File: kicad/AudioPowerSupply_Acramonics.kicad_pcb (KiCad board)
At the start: 2 copper layers, 33 parts, among them J6 GND 48V, J7 Conn_01x03_Pin, J8 Conn_01x03_Pin, U1 LM7815_TO220, U2 LM7915_TO220, U3 LM317_TO-220

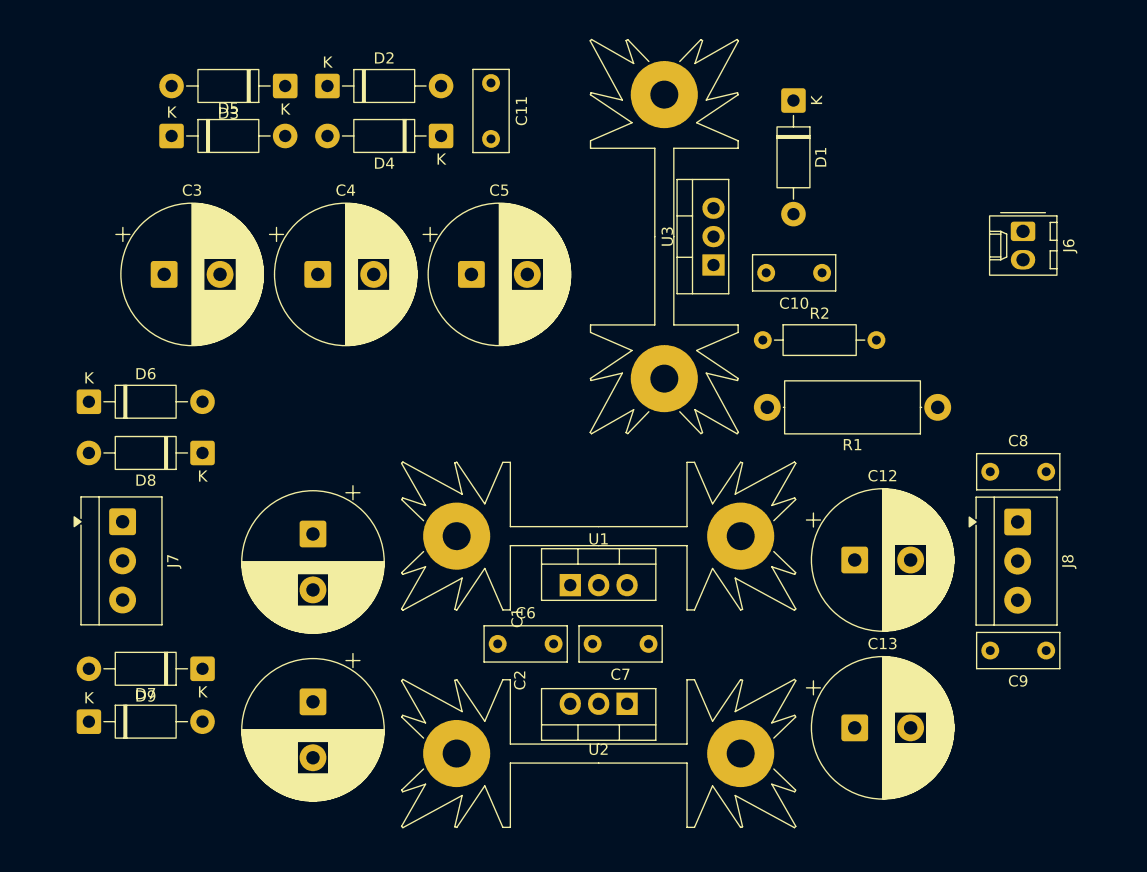
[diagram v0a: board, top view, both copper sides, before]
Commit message: Put 48V circuit on separate diagram
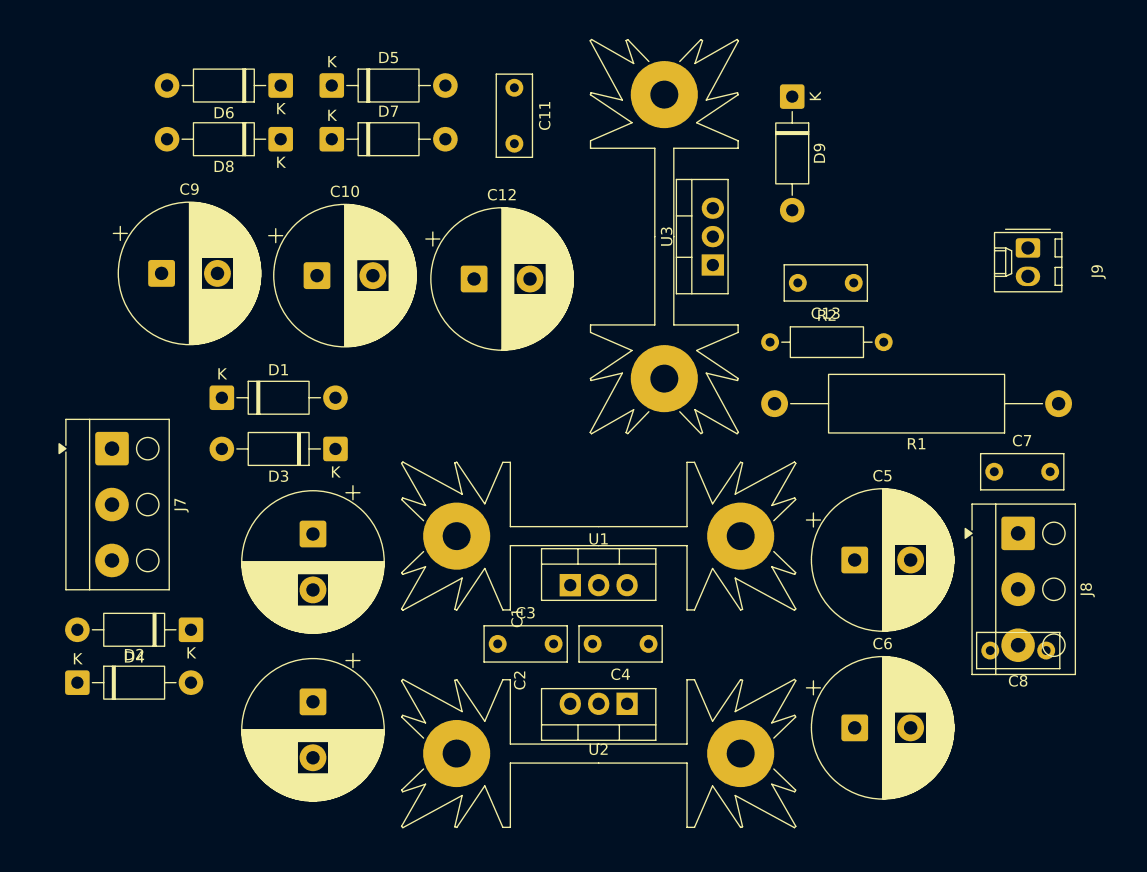
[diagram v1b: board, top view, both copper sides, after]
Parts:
- removed the C3 at (69.0, 88.7)
- removed the C4 at (82.7, 88.7)
- removed the C5 at (96.5, 88.7)
- removed the D1 at (125.3, 73.2)
- removed the D2 at (83.6, 71.9)
- removed the D3 at (79.8, 71.9)
- removed the D4 at (93.7, 76.4)
- removed J6: GND 48V, Connector_Molex:Molex_KK-254_AE-6410-02A_1x02_P2.54mm_Vertical
- added C12: 220uF 100V, Capacitor_THT:CP_Radial_D12.5mm_P5.00mm, F.Cu at (96.7, 89.2)
- added C13: 100nF, Capacitor_THT:C_Rect_L7.2mm_W3.0mm_P5.00mm_FKS2_FKP2_MKS2_MKP2, F.Cu at (130.7, 89.5)
- added C9: 100uF 100V, Capacitor_THT:CP_Radial_D12.5mm_P5.00mm, F.Cu at (68.8, 88.7)
- added D6: 1N4004, Diode_THT:D_DO-41_SOD81_P10.16mm_Horizontal, F.Cu at (79.4, 71.8)
- added D7: 1N4004, Diode_THT:D_DO-41_SOD81_P10.16mm_Horizontal, F.Cu at (84.0, 76.7)
- added D8: 1N4004, Diode_THT:D_DO-41_SOD81_P10.16mm_Horizontal, F.Cu at (79.4, 76.7)
- added D9: 1N4003, Diode_THT:D_DO-41_SOD81_P10.16mm_Horizontal, F.Cu at (125.2, 72.8)
- added J9: 48V out, Connector_Molex:Molex_KK-254_AE-6410-02A_1x02_P2.54mm_Vertical, F.Cu at (146.2, 86.4)
- C10: value 100nF -> 100uF 100V; footprint Capacitor_THT:C_Rect_L7.2mm_W3.0mm_P5.00mm_FKS2_FKP2_MKS2_MKP2 -> Capacitor_THT:CP_Radial_D12.5mm_P5.00mm
- J7, J8: footprint TerminalBlock_4Ucon:TerminalBlock_4Ucon_1x03_P3.50mm_Horizontal -> TerminalBlock_Altech:Altech_AK100_1x03_P5.00mm
- R1: footprint Resistor_THT:R_Axial_DIN0414_L11.9mm_D4.5mm_P15.24mm_Horizontal -> Resistor_THT:R_Axial_DIN0516_L15.5mm_D5.0mm_P25.40mm_Horizontal
- moved C10 45.2 mm to (82.7, 88.8), turned to 0 degrees
- moved D5 15.0 mm to (84.0, 71.8)
- moved D1 11.9 mm to (74.1, 99.8)
- moved D3 11.9 mm to (84.3, 104.3)
- moved R1 10.8 mm to (149.0, 100.3)
- moved J7 6.60 mm to (64.3, 104.3)
- moved D4 3.64 mm to (71.4, 120.5)
- moved D2 3.64 mm to (61.2, 125.2)
- moved C11 2.13 mm to (100.3, 72.0)
- moved J8 1.02 mm to (145.3, 111.9)
- moved R2 0.68 mm to (123.2, 94.8)
- moved C7 0.36 mm to (143.2, 106.4)
- moved U3 0.06 mm to (118.0, 87.9)
- renumbered C6 to C3, C7 to C4, C12 to C5, C13 to C6, C8 to C7, C9 to C8, D6 to D1, D7 to D2, D8 to D3, D9 to D4
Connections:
- C10 pad 1: GND -> Net-(D6-K)
- C10 pad 2: +48V -> AC17-

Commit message: Board done - needs added text
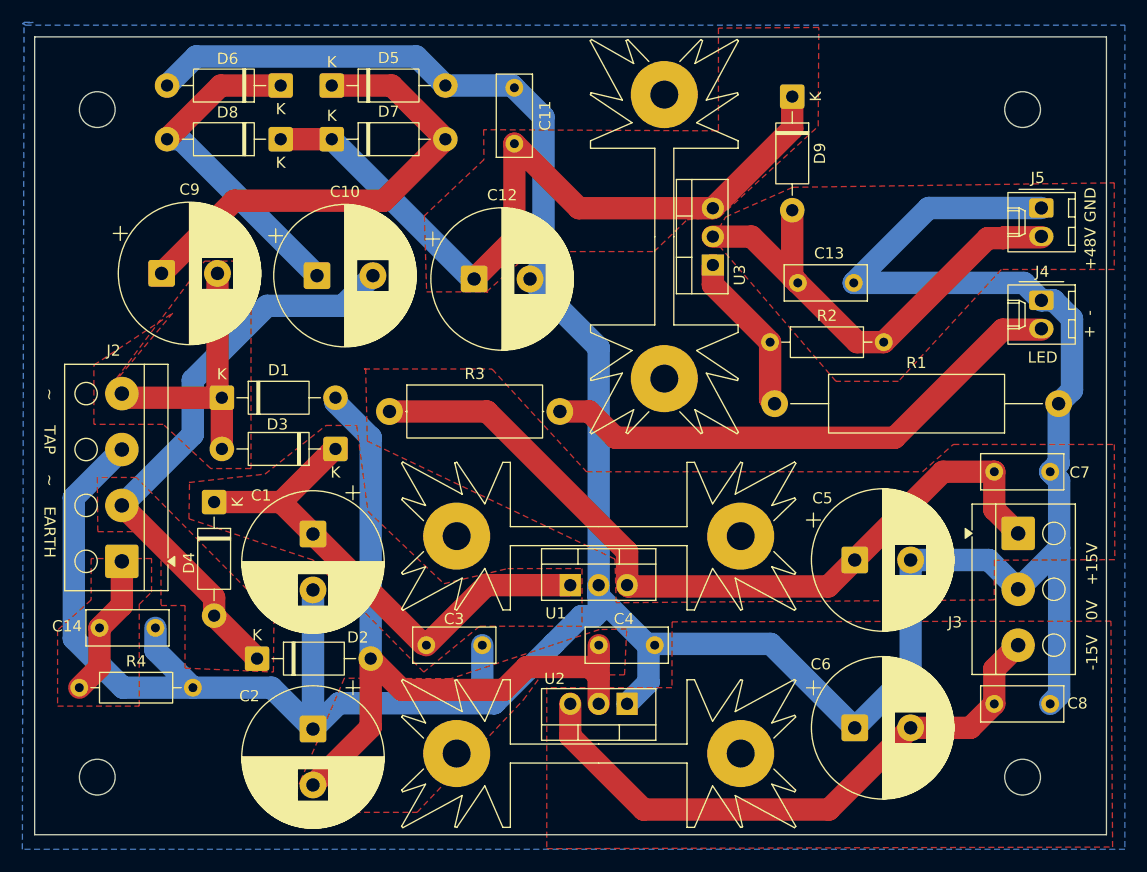
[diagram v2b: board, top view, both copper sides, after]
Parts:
- removed J7: Conn_01x03_Pin, TerminalBlock_Altech:Altech_AK100_1x03_P5.00mm
- added C14: 10nF, Capacitor_THT:C_Rect_L7.2mm_W3.0mm_P5.00mm_FKS2_FKP2_MKS2_MKP2, F.Cu at (63.2, 120.3)
- added J2: Conn_01x04_Pin, TerminalBlock_Altech:Altech_AK100_1x04_P5.00mm, F.Cu at (65.2, 114.4)
- added J4: ~, Connector_Molex:Molex_KK-254_AE-6410-02A_1x02_P2.54mm_Vertical, F.Cu at (147.4, 91.1)
- added R3: 3K6 1W, Resistor_THT:R_Axial_DIN0414_L11.9mm_D4.5mm_P15.24mm_Horizontal, F.Cu at (89.1, 101.0)
- added R4: 1K, Resistor_THT:R_Axial_DIN0207_L6.3mm_D2.5mm_P10.16mm_Horizontal, F.Cu at (61.4, 125.7)
- added REF**: MountingHole_3.2mm_M3, MountingHole:MountingHole_3.2mm_M3, F.Cu at (63.0, 74.0)
- added REF**: MountingHole_3.2mm_M3, MountingHole:MountingHole_3.2mm_M3, F.Cu at (145.8, 133.7)
- added REF**: MountingHole_3.2mm_M3, MountingHole:MountingHole_3.2mm_M3, F.Cu at (145.8, 74.0)
- added REF**: MountingHole_3.2mm_M3, MountingHole:MountingHole_3.2mm_M3, F.Cu at (63.0, 133.7)
- J3: renamed from J8; value Conn_01x03_Pin -> ~
- moved D2 16.2 mm to (77.3, 123.1)
- moved D4 11.6 mm to (73.5, 109.1), turned to -90 degrees
- moved C3 6.38 mm to (92.4, 121.9)
- moved C8 4.79 mm to (148.2, 127.2)
- moved J5 3.77 mm to (147.4, 82.8)
- moved C2 2.43 mm to (82.3, 129.4)
- moved C4 0.56 mm to (112.8, 121.9)
- renumbered J9 to J5
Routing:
- net GND: track 0.00 -> 326.6 mm
- net +15V: track 0.00 -> 73.0 mm
- net Net-(D7-K): track 0.00 -> 69.1 mm
- net Net-(D1-A): track 0.00 -> 66.0 mm
- net -15V: track 0.00 -> 53.6 mm
- net AC17-: track 0.00 -> 52.5 mm
- net Net-(J4-Pin_2): track 0.00 -> 48.0 mm
- net Net-(D3-K): track 0.00 -> 45.9 mm
- net +48V: track 0.00 -> 43.9 mm
- net Net-(D5-K): track 0.00 -> 42.5 mm
- net Net-(D6-K): track 0.00 -> 30.6 mm
- net AC17+: track 0.00 -> 25.0 mm
- net Net-(U3-ADJ): track 0.00 -> 14.7 mm
- net GNDPWR: track 0.00 -> 12.9 mm
- added copper zone on F.Cu, net +15V
- added copper zone on F.Cu, net +48V
- added copper zone on F.Cu, net -15V
- added copper zone on F.Cu, net AC17+
- added copper zone on F.Cu, net AC17-
- added copper zone on B.Cu, net GND
- added copper zone on F.Cu, net GNDPWR
- added copper zone on F.Cu, net Net-(D1-A)
- added copper zone on F.Cu, net Net-(D3-K)
- added copper zone on F.Cu, net Net-(D7-K)
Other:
- board outline added: 95.8 x 71.3 mm
- board text added: "+ -"
- board text added: "+48V GND"
- board text added: "-15V 0V +15V"
- board text added: "LED"
- board text added: "~ TAP ~ EARTH"

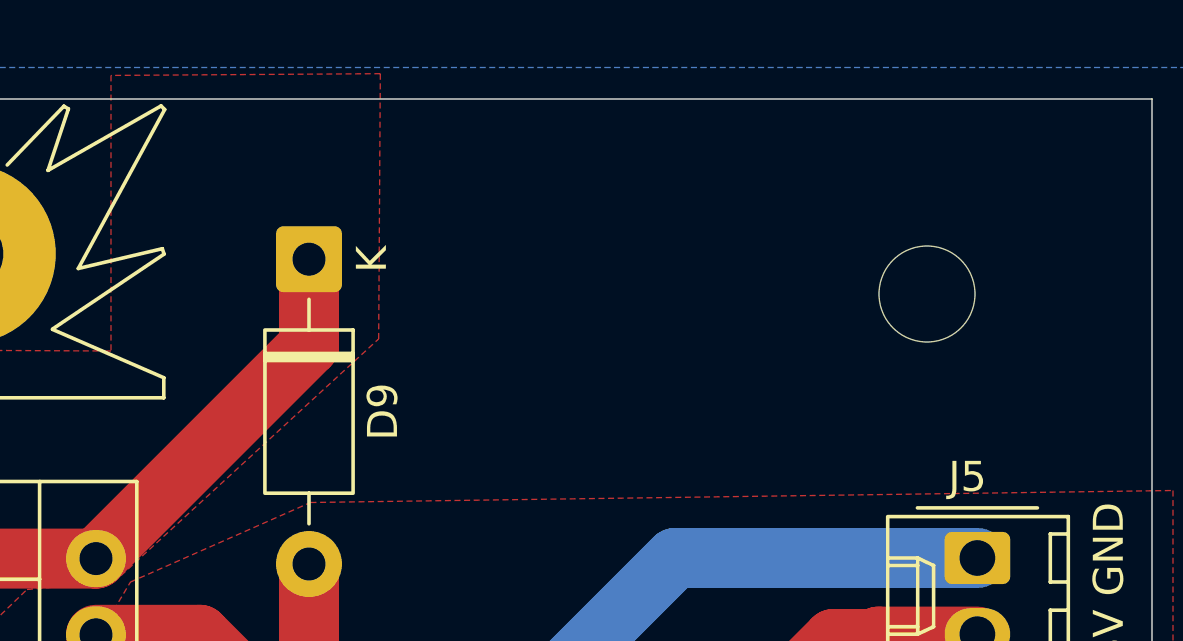
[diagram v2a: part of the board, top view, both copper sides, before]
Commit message: Added text and updated readme
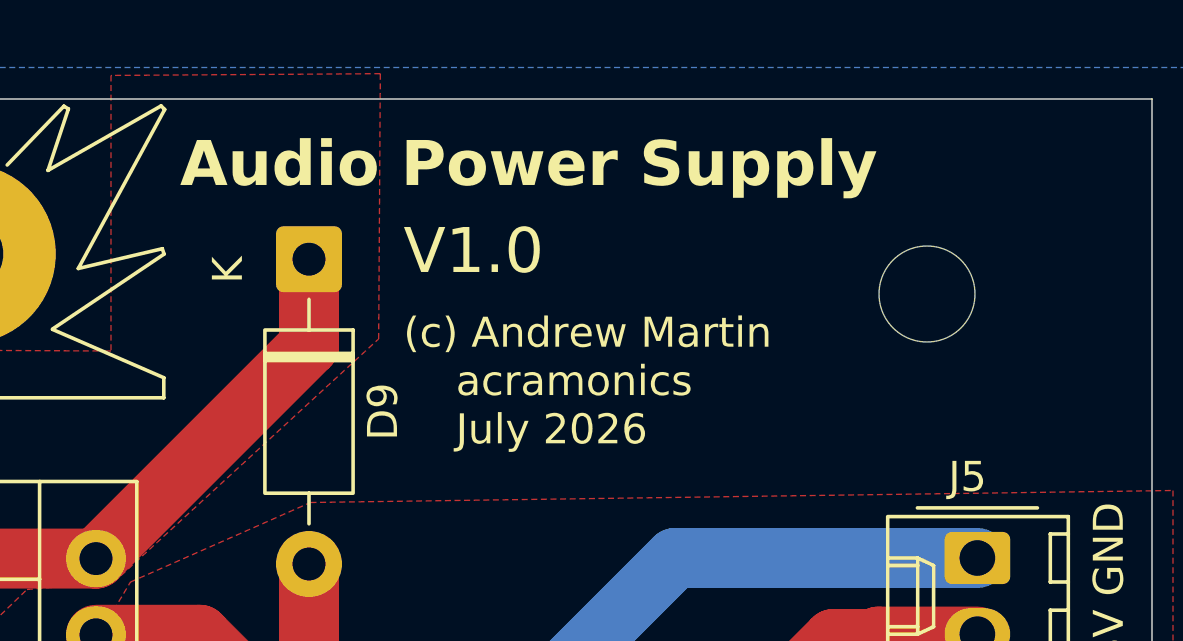
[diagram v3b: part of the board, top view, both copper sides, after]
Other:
- board text added: "(c) Andrew Martin acramonics July 2026"
- board text added: "Audio Power Supply"
- board text added: "V1.0"
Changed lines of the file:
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@@
 		)
 		(fp_text user "K"
-			(at 0 -2.1 90)
+			(at 0.36 2.7 90)
 			(layer "F.SilkS")
 			(effects
@@
 		(layer "Edge.Cuts")
 	)
+	(gr_text "(c) Andrew Martin\n    acramonics\n    July 2026"
+		(at 128.3 79.1 0)
+		(layer "F.SilkS")
+		(effects
+			(font
+				(size 1 1)
+				(thickness 0.1)
+			)
+			(justify left bottom)
+		)
+	)
 	(gr_text "LED"
 		(at 146.2 96.75 0)
@@
 		)
 	)
+	(gr_text "V1.0"
+		(at 128.3 73.45 0)
+		(layer "F.SilkS")
+		(effects
+			(font
+				(size 1.5 1.5)
+				(thickness 0.1875)
+			)
+			(justify left bottom)
+		)
+	)
+	(gr_text "Audio Power Supply"
+		(at 120.85 70.55 0)
+		(layer "F.SilkS")
+		(effects
+			(font
+				(size 1.5 1.5)
+				(thickness 0.3)
+				(bold yes)
+			)
+			(justify left bottom)
+		)
+	)
 	(segment
 		(start 79.4 71.85)
@@
 	)
 	(segment
+		(start 130.736041 114.28)
+		(end 138.627736 106.388305)
+		(width 2)
+		(layer "F.Cu")
+		(net "+15V")
+	)
+	(segment
+		(start 110.38 113.53)
+		(end 110.38 116.53)
+		(width 2)
+		(layer "F.Cu")
+		(net "+15V")
+	)
+	(segment
+		(start 89.13 101)
+		(end 97.85 101)
+		(width 2)
+		(layer "F.Cu")
+		(net "+15V")
+	)
+	(segment
+		(start 128.369346 116.646695)
+		(end 130.736041 114.28)
+		(width 2)
+		(layer "F.Cu")
+		(net "+15V")
+	)
+	(segment
+		(start 110.496695 116.646695)
+		(end 128.369346 116.646695)
+		(width 2)
+		(layer "F.Cu")
+		(net "+15V")
+	)
+	(segment
+		(start 97.85 101)
+		(end 110.38 113.53)
+		(width 2)
+		(layer "F.Cu")
+		(net "+15V")
+	)
+	(segment
+		(start 138.627736 106.388305)
+		(end 143.2175 106.388305)
+		(width 2)
+		(layer "F.Cu")
+		(net "+15V")
+	)
+	(segment
+		(start 110.38 116.53)
+		(end 110.496695 116.646695)
+		(width 2)
+		(layer "F.Cu")
+		(net "+15V")
+	)
+	(segment
+		(start 143.2175 109.7675)
+		(end 145.35 111.9)
+		(width 2)
+		(layer "F.Cu")
+		(net "+15V")
+	)
+	(segment
+		(start 143.2175 106.388305)
+		(end 143.2175 109.7675)
+		(width 2)
+		(layer "F.Cu")
+		(net "+15V")
+	)
+	(segment
+		(start 143.97 93.68)
+		(end 147.43 93.68)
+		(width 2)
+		(layer "F.Cu")
+		(net "Net-(J4-Pin_2)")
+	)
+	(segment
+		(start 107 101)
+		(end 109.35 103.35)
+		(width 2)
+		(layer "F.Cu")
+		(net "Net-(J4-Pin_2)")
+	)
+	(segment
+		(start 104.37 101)
+		(end 107 101)
+		(width 2)
+		(layer "F.Cu")
+		(net "Net-(J4-Pin_2)")
+	)
+	(segment
+		(start 134.3 103.35)
+		(end 143.97 93.68)
+		(width 2)
+		(layer "F.Cu")
+		(net "Net-(J4-Pin_2)")
+	)
+	(segment
+		(start 109.35 103.35)
+		(end 134.3 103.35)
+		(width 2)
+		(layer "F.Cu")
+		(net "Net-(J4-Pin_2)")
+	)
+	(segment
 		(start 123.17 94.8)
 		(end 123.17 99.9)
@@
 	)
 	(segment
-		(start 73.75 88.65)
-		(end 73.75 99.38)
+		(start 63.2 120.35)
+		(end 63.2 123.89)
 		(width 2)
 		(layer "F.Cu")
-		(net "AC17+")
+		(net "GNDPWR")
 	)
 	(segment
-		(start 73.75 99.38)
-		(end 74.14 99.77)
+		(start 65.2 114.4)
+		(end 65.2 118.35)
 		(width 2)
 		(layer "F.Cu")
-		(net "AC17+")
+		(net "GNDPWR")
 	)
 	(segment
-		(start 65.57 99.77)
-		(end 65.2 99.4)
+		(start 65.2 118.35)
+		(end 63.2 120.35)
 		(width 2)
 		(layer "F.Cu")
-		(net "AC17+")
+		(net "GNDPWR")
 	)
 	(segment
-		(start 74.14 99.77)
-		(end 65.57 99.77)
+		(start 63.2 123.89)
+		(end 61.39 125.7)
 		(width 2)
 		(layer "F.Cu")
-		(net "AC17+")
+		(net "GNDPWR")
 	)
 	(segment
-		(start 74.14 99.77)
-		(end 74.14 104.35)
+		(start 73.75 88.65)
+		(end 73.75 99.38)
 		(width 2)
 		(layer "F.Cu")
@@
 	)
 	(segment
-		(start 130.736041 114.28)
-		(end 138.627736 106.388305)
-		(width 2)
-		(layer "F.Cu")
-		(net "+15V")
-	)
-	(segment
-		(start 110.38 113.53)
-		(end 110.38 116.53)
-		(width 2)
-		(layer "F.Cu")
-		(net "+15V")
-	)
-	(segment
-		(start 89.13 101)
-		(end 97.85 101)
-		(width 2)
-		(layer "F.Cu")
-		(net "+15V")
-	)
-	(segment
-		(start 128.369346 116.646695)
-		(end 130.736041 114.28)
-		(width 2)
-		(layer "F.Cu")
-		(net "+15V")
-	)
-	(segment
-		(start 110.496695 116.646695)
-		(end 128.369346 116.646695)
-		(width 2)
-		(layer "F.Cu")
-		(net "+15V")
-	)
-	(segment
-		(start 97.85 101)
-		(end 110.38 113.53)
-		(width 2)
-		(layer "F.Cu")
-		(net "+15V")
-	)
-	(segment
-		(start 138.627736 106.388305)
-		(end 143.2175 106.388305)
+		(start 73.75 99.38)
+		(end 74.14 99.77)
 		(width 2)
 		(layer "F.Cu")
-		(net "+15V")
+		(net "AC17+")
 	)
 	(segment
-		(start 110.38 116.53)
-		(end 110.496695 116.646695)
+		(start 65.57 99.77)
+		(end 65.2 99.4)
 		(width 2)
 		(layer "F.Cu")
-		(net "+15V")
+		(net "AC17+")
 	)
 	(segment
-		(start 143.2175 109.7675)
-		(end 145.35 111.9)
+		(start 74.14 99.77)
+		(end 65.57 99.77)
 		(width 2)
 		(layer "F.Cu")
-		(net "+15V")
+		(net "AC17+")
 	)
 	(segment
-		(start 143.2175 106.388305)
-		(end 143.2175 109.7675)
+		(start 74.14 99.77)
+		(end 74.14 104.35)
 		(width 2)
 		(layer "F.Cu")
-		(net "+15V")
+		(net "AC17+")
 	)
 	(segment
@@
 		(net "Net-(D5-K)")
 	)
-	(segment
-		(start 63.2 120.35)
-		(end 63.2 123.89)
-		(width 2)
-		(layer "F.Cu")
-		(net "GNDPWR")
-	)
-	(segment
-		(start 65.2 114.4)
-		(end 65.2 118.35)
-		(width 2)
-		(layer "F.Cu")
-		(net "GNDPWR")
-	)
-	(segment
-		(start 65.2 118.35)
-		(end 63.2 120.35)
-		(width 2)
-		(layer "F.Cu")
-		(net "GNDPWR")
-	)
-	(segment
-		(start 63.2 123.89)
-		(end 61.39 125.7)
-		(width 2)
-		(layer "F.Cu")
-		(net "GNDPWR")
-	)
-	(segment
-		(start 143.97 93.68)
-		(end 147.43 93.68)
-		(width 2)
-		(layer "F.Cu")
-		(net "Net-(J4-Pin_2)")
-	)
-	(segment
-		(start 107 101)
-		(end 109.35 103.35)
-		(width 2)
-		(layer "F.Cu")
-		(net "Net-(J4-Pin_2)")
-	)
-	(segment
-		(start 104.37 101)
-		(end 107 101)
-		(width 2)
-		(layer "F.Cu")
-		(net "Net-(J4-Pin_2)")
-	)
-	(segment
-		(start 134.3 103.35)
-		(end 143.97 93.68)
-		(width 2)
-		(layer "F.Cu")
-		(net "Net-(J4-Pin_2)")
-	)
-	(segment
-		(start 109.35 103.35)
-		(end 134.3 103.35)
-		(width 2)
-		(layer "F.Cu")
-		(net "Net-(J4-Pin_2)")
-	)
 	(zone
